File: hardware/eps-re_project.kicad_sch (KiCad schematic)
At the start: 14 parts, among them J1 53398-0471, J10 53398-0471, J11 53398-0471, J12 53398-0671, J13 53398-0671, J14 53398-0471, J2 53398-0471, J3 53398-0671, J4 53398-0471, J5 53398-0471, J6 53398-0471, J7 53398-0471, J8 53398-0671, J9 53398-0471

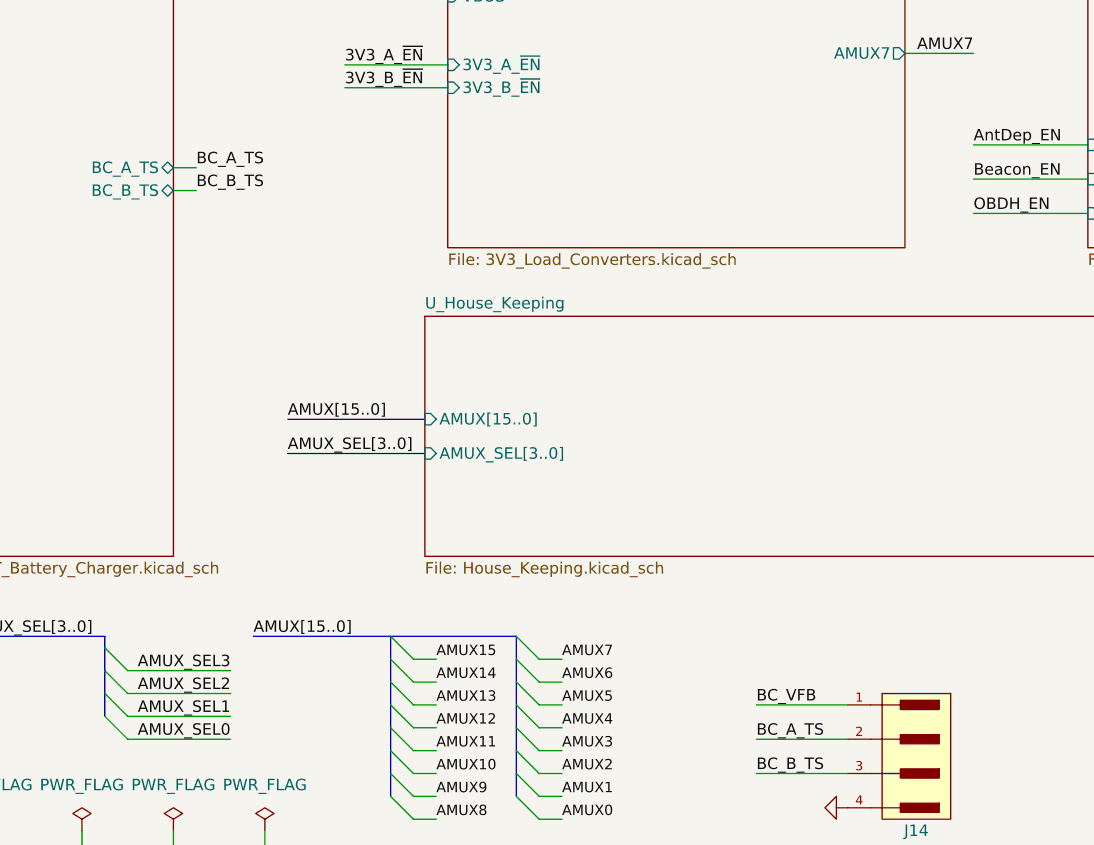
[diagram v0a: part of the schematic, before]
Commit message: hardware: Updating the schematic considering issues #2, #3, #4, #5 and #6.
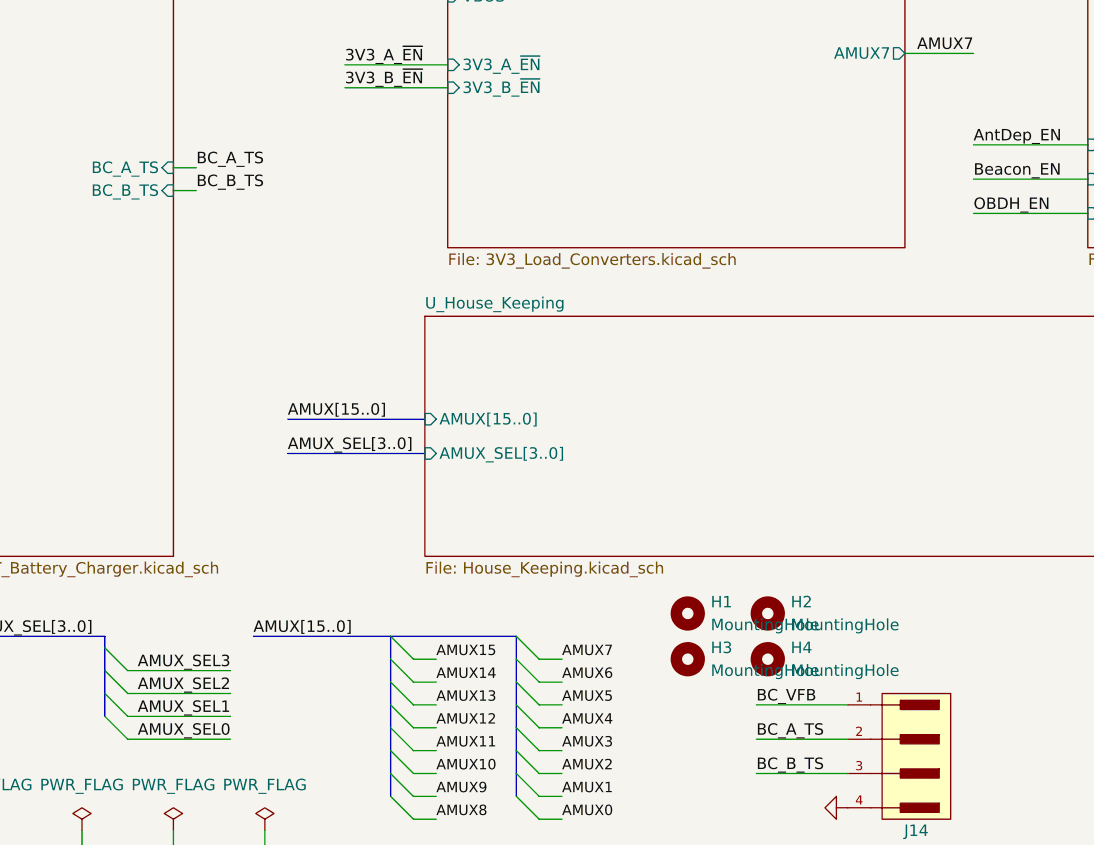
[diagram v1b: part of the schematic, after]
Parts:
- added H1, H2, H3, H4: MountingHole, MountingHole:MountingHole_3.2mm_M3_ISO14580_Pad, symbol Mechanical:MountingHole
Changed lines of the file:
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@@
+    )
+  )
+  (symbol (lib_id "Mechanical:MountingHole") (at 151.13 172.72 0) (unit 1)
+    (in_bom yes) (on_board yes) (dnp no) (fields_autoplaced)
+    (property "Reference" "H4" (at 153.67 171.45 0)
+      (effects (font (size 1.27 1.27)) (justify left))
+    )
+    (property "Value" "MountingHole" (at 153.67 173.99 0)
+      (effects (font (size 1.27 1.27)) (justify left))
+    )
+    (property "Footprint" "MountingHole:MountingHole_3.2mm_M3_ISO14580_Pad" (at 151.13 172.72 0)
+      (effects (font (size 1.27 1.27)) hide)
+    )
+    (property "Datasheet" "~" (at 151.13 172.72 0)
+      (effects (font (size 1.27 1.27)) hide)
+    )
+    (instances
+      (project "eps-re_project"
+        (path "/2eebaa11-d7ed-4bfd-bc8e-988f68654d29"
+          (reference "H4") (unit 1)
+        )
+      )
     )
   )
@@
         (path "/2eebaa11-d7ed-4bfd-bc8e-988f68654d29"
           (reference "#PWR0119") (unit 1)
+        )
+      )
+    )
+  )
+  (symbol (lib_id "Mechanical:MountingHole") (at 142.24 172.72 0) (unit 1)
+    (in_bom yes) (on_board yes) (dnp no) (fields_autoplaced)
+    (property "Reference" "H3" (at 144.78 171.45 0)
+      (effects (font (size 1.27 1.27)) (justify left))
+    )
+    (property "Value" "MountingHole" (at 144.78 173.99 0)
+      (effects (font (size 1.27 1.27)) (justify left))
+    )
+    (property "Footprint" "MountingHole:MountingHole_3.2mm_M3_ISO14580_Pad" (at 142.24 172.72 0)
+      (effects (font (size 1.27 1.27)) hide)
+    )
+    (property "Datasheet" "~" (at 142.24 172.72 0)
+      (effects (font (size 1.27 1.27)) hide)
+    )
+    (instances
+      (project "eps-re_project"
+        (path "/2eebaa11-d7ed-4bfd-bc8e-988f68654d29"
+          (reference "H3") (unit 1)
         )
       )
@@
         (path "/2eebaa11-d7ed-4bfd-bc8e-988f68654d29"
           (reference "#PWR035") (unit 1)
+        )
+      )
+    )
+  )
+  (symbol (lib_id "Mechanical:MountingHole") (at 151.13 167.64 0) (unit 1)
+    (in_bom yes) (on_board yes) (dnp no) (fields_autoplaced)
+    (property "Reference" "H2" (at 153.67 166.37 0)
+      (effects (font (size 1.27 1.27)) (justify left))
+    )
+    (property "Value" "MountingHole" (at 153.67 168.91 0)
+      (effects (font (size 1.27 1.27)) (justify left))
+    )
+    (property "Footprint" "MountingHole:MountingHole_3.2mm_M3_ISO14580_Pad" (at 151.13 167.64 0)
+      (effects (font (size 1.27 1.27)) hide)
+    )
+    (property "Datasheet" "~" (at 151.13 167.64 0)
+      (effects (font (size 1.27 1.27)) hide)
+    )
+    (instances
+      (project "eps-re_project"
+        (path "/2eebaa11-d7ed-4bfd-bc8e-988f68654d29"
+          (reference "H2") (unit 1)
         )
       )
@@
     )
   )
+  (symbol (lib_id "Mechanical:MountingHole") (at 142.24 167.64 0) (unit 1)
+    (in_bom yes) (on_board yes) (dnp no) (fields_autoplaced)
+    (property "Reference" "H1" (at 144.78 166.37 0)
+      (effects (font (size 1.27 1.27)) (justify left))
+    )
+    (property "Value" "MountingHole" (at 144.78 168.91 0)
+      (effects (font (size 1.27 1.27)) (justify left))
+    )
+    (property "Footprint" "MountingHole:MountingHole_3.2mm_M3_ISO14580_Pad" (at 142.24 167.64 0)
+      (effects (font (size 1.27 1.27)) hide)
+    )
+    (property "Datasheet" "~" (at 142.24 167.64 0)
+      (effects (font (size 1.27 1.27)) hide)
+    )
+    (instances
+      (project "eps-re_project"
+        (path "/2eebaa11-d7ed-4bfd-bc8e-988f68654d29"
+          (reference "H1") (unit 1)
+        )
+      )
+    )
+  )
   (symbol (lib_id "533980471:533980471_1") (at 33.02 30.48 0) (unit 1)
     (in_bom yes) (on_board yes) (dnp no)
@@
       (effects (font (size 1.27 1.27)) (justify left))
     )
-    (pin "BC_A_TS" bidirectional (at 85.09 118.11 0)
+    (pin "BC_A_TS" input (at 85.09 118.11 0)
       (effects (font (size 1.27 1.27)) (justify right))
     )
@@
       (effects (font (size 1.27 1.27)) (justify left))
     )
-    (pin "BC_B_TS" bidirectional (at 85.09 120.65 0)
+    (pin "BC_B_TS" input (at 85.09 120.65 0)
       (effects (font (size 1.27 1.27)) (justify right))
     )

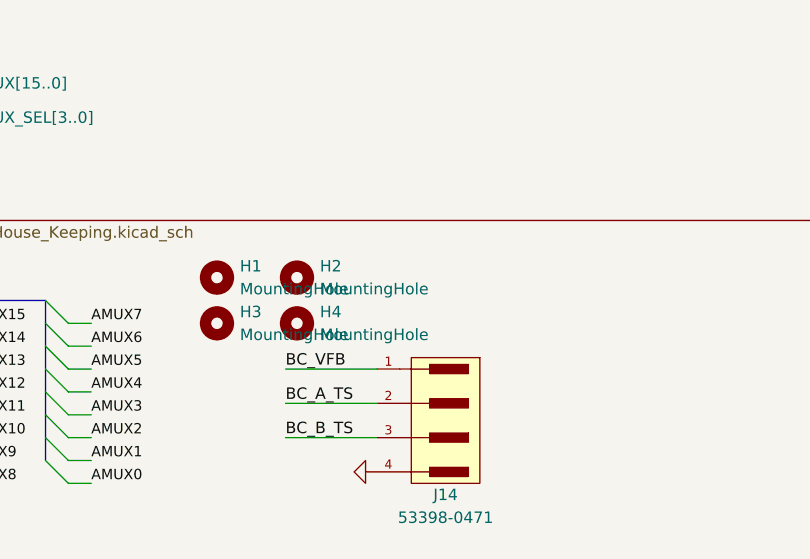
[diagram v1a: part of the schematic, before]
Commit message: hardware: Updating 3D models, component placement and more.
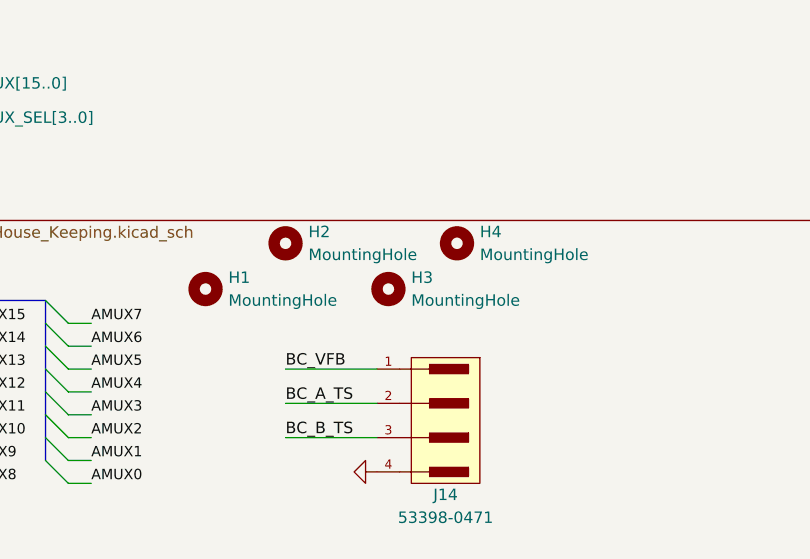
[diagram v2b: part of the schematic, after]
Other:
- title: (none) -> Reliability Enhanced Electrical Power System
- moved on the sheet: H1, H2, H3, H4
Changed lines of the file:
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@@
 (kicad_sch (version 20230121) (generator eeschema)
   (paper "A4")
+  (title_block
+    (title "Reliability Enhanced Electrical Power System")
+    (date "2023-08-03")
+    (rev "v0.0")
+    (comment 1 "João C. E. Barcellos <joaoclaudiobarcellos@gmail.com>")
+    (comment 2 "Laura Debastiani <laudebastiani@gmail.com>")
+  )
   (junction (at 36.83 33.02) (diameter 0) (color 0 0 0 0)
   )
@@
     )
   )
-  (symbol (lib_id "Mechanical:MountingHole") (at 151.13 172.72 0) (unit 1)
+  (symbol (lib_id "Mechanical:MountingHole") (at 168.91 163.83 0) (unit 1)
     (in_bom yes) (on_board yes) (dnp no) (fields_autoplaced)
-    (property "Reference" "H4" (at 153.67 171.45 0)
+    (property "Reference" "H4" (at 171.45 162.56 0)
       (effects (font (size 1.27 1.27)) (justify left))
     )
-    (property "Value" "MountingHole" (at 153.67 173.99 0)
+    (property "Value" "MountingHole" (at 171.45 165.1 0)
       (effects (font (size 1.27 1.27)) (justify left))
     )
-    (property "Footprint" "MountingHole:MountingHole_3.2mm_M3_ISO14580_Pad" (at 151.13 172.72 0)
-      (effects (font (size 1.27 1.27)) hide)
-    )
-    (property "Datasheet" "~" (at 151.13 172.72 0)
+    (property "Footprint" "MountingHole:MountingHole_3.2mm_M3_ISO14580_Pad" (at 168.91 163.83 0)
+      (effects (font (size 1.27 1.27)) hide)
+    )
+    (property "Datasheet" "~" (at 168.91 163.83 0)
       (effects (font (size 1.27 1.27)) hide)
     )
@@
     )
   )
-  (symbol (lib_id "Mechanical:MountingHole") (at 142.24 172.72 0) (unit 1)
+  (symbol (lib_id "Mechanical:MountingHole") (at 161.29 168.91 0) (unit 1)
     (in_bom yes) (on_board yes) (dnp no) (fields_autoplaced)
-    (property "Reference" "H3" (at 144.78 171.45 0)
+    (property "Reference" "H3" (at 163.83 167.64 0)
       (effects (font (size 1.27 1.27)) (justify left))
     )
-    (property "Value" "MountingHole" (at 144.78 173.99 0)
+    (property "Value" "MountingHole" (at 163.83 170.18 0)
       (effects (font (size 1.27 1.27)) (justify left))
     )
-    (property "Footprint" "MountingHole:MountingHole_3.2mm_M3_ISO14580_Pad" (at 142.24 172.72 0)
-      (effects (font (size 1.27 1.27)) hide)
-    )
-    (property "Datasheet" "~" (at 142.24 172.72 0)
+    (property "Footprint" "MountingHole:MountingHole_3.2mm_M3_ISO14580_Pad" (at 161.29 168.91 0)
+      (effects (font (size 1.27 1.27)) hide)
+    )
+    (property "Datasheet" "~" (at 161.29 168.91 0)
       (effects (font (size 1.27 1.27)) hide)
     )
@@
     )
   )
-  (symbol (lib_id "Mechanical:MountingHole") (at 151.13 167.64 0) (unit 1)
+  (symbol (lib_id "Mechanical:MountingHole") (at 149.86 163.83 0) (unit 1)
     (in_bom yes) (on_board yes) (dnp no) (fields_autoplaced)
-    (property "Reference" "H2" (at 153.67 166.37 0)
+    (property "Reference" "H2" (at 152.4 162.56 0)
       (effects (font (size 1.27 1.27)) (justify left))
     )
-    (property "Value" "MountingHole" (at 153.67 168.91 0)
+    (property "Value" "MountingHole" (at 152.4 165.1 0)
       (effects (font (size 1.27 1.27)) (justify left))
     )
-    (property "Footprint" "MountingHole:MountingHole_3.2mm_M3_ISO14580_Pad" (at 151.13 167.64 0)
-      (effects (font (size 1.27 1.27)) hide)
-    )
-    (property "Datasheet" "~" (at 151.13 167.64 0)
+    (property "Footprint" "MountingHole:MountingHole_3.2mm_M3_ISO14580_Pad" (at 149.86 163.83 0)
+      (effects (font (size 1.27 1.27)) hide)
+    )
+    (property "Datasheet" "~" (at 149.86 163.83 0)
       (effects (font (size 1.27 1.27)) hide)
     )
@@
     )
   )
-  (symbol (lib_id "Mechanical:MountingHole") (at 142.24 167.64 0) (unit 1)
+  (symbol (lib_id "Mechanical:MountingHole") (at 140.97 168.91 0) (unit 1)
     (in_bom yes) (on_board yes) (dnp no) (fields_autoplaced)
-    (property "Reference" "H1" (at 144.78 166.37 0)
+    (property "Reference" "H1" (at 143.51 167.64 0)
       (effects (font (size 1.27 1.27)) (justify left))
     )
-    (property "Value" "MountingHole" (at 144.78 168.91 0)
+    (property "Value" "MountingHole" (at 143.51 170.18 0)
       (effects (font (size 1.27 1.27)) (justify left))
     )
-    (property "Footprint" "MountingHole:MountingHole_3.2mm_M3_ISO14580_Pad" (at 142.24 167.64 0)
-      (effects (font (size 1.27 1.27)) hide)
-    )
-    (property "Datasheet" "~" (at 142.24 167.64 0)
-      (effects (font (size 1.27 1.27)) hide)
-    )
+    (property "Footprint" "MountingHole:MountingHole_3.2mm_M3_ISO14580_Pad" (at 140.97 168.91 0)
+      (effects (font (size 1.27 1.27)) hide)
+    )
+    (property "Datasheet" "~" (at 140.97 168.91 0)
+      (effects (font (size 1.27 1.27)) hide)
+    )

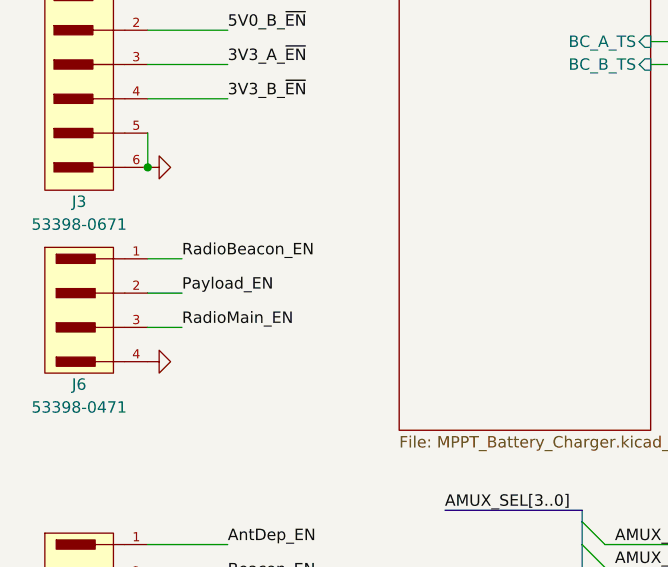
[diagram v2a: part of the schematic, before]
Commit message: hardware: Adding some 3D models, changing the placement of components and routing more nets.
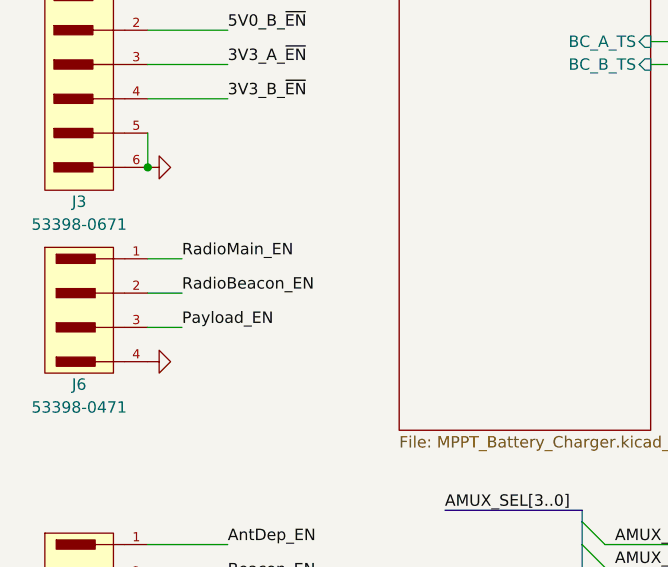
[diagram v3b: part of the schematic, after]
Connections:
- net Payload_EN: now also J6.3; no longer J6.2
- net RadioBeacon_EN: now also J6.2; no longer J6.1
- net RadioMain_EN: now also J6.1; no longer J6.3

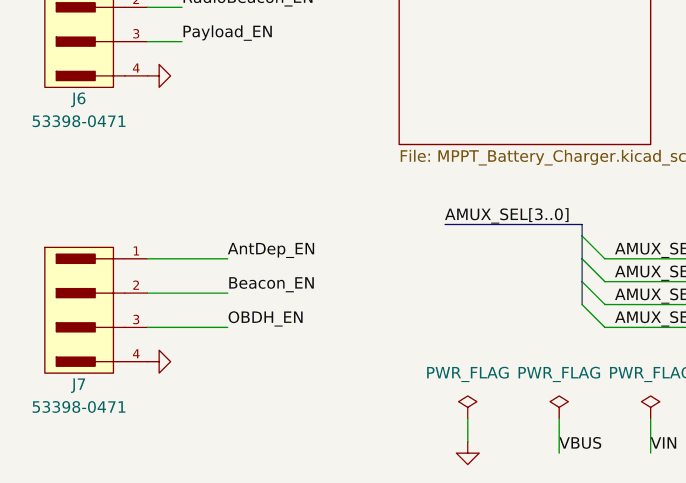
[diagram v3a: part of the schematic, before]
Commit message: hardware: Updating footprint references size.
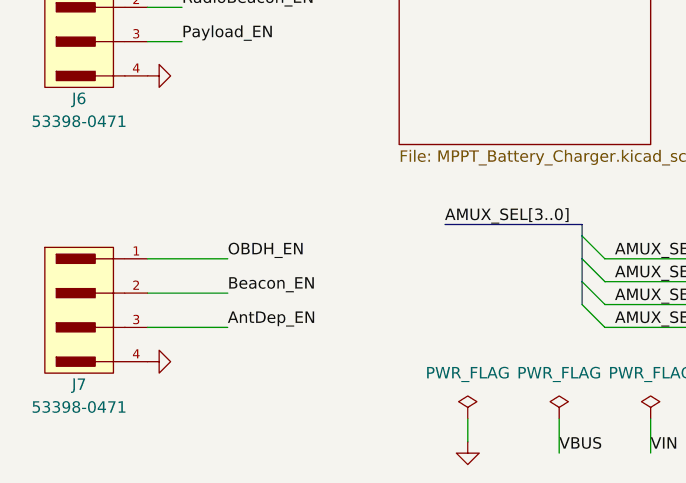
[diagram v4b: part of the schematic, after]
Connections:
- net AntDep_EN: now also J7.3; no longer J7.1
- net OBDH_EN: now also J7.1; no longer J7.3
